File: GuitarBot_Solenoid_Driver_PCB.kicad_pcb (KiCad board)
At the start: 2 copper layers, 123.2 x 109.2 mm, 89 parts, among them J3V3 Screw_Terminal_01x02, Q1 NMOS, Q10 NMOS, Q11 NMOS, Q12 NMOS, Q13 NMOS, Q14 NMOS, Q15 NMOS, Q16 NMOS, Q2 NMOS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

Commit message: fixed labels:
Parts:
- moved D8 3.03 mm to (153.7, 99.1)
- moved D7 2.60 mm to (153.7, 105.5)
- moved D9 2.22 mm to (153.7, 92.7)
- moved D6 2.17 mm to (153.7, 112.0)
- moved D10 1.90 mm to (153.7, 86.2)
- moved D5 1.73 mm to (153.7, 118.4)
- moved D11 1.58 mm to (153.7, 79.8)
- moved D4 1.30 mm to (153.7, 124.8)
- moved D12 1.27 mm to (153.7, 73.4)
- moved D13 0.95 mm to (153.7, 66.9)
- moved D3 0.87 mm to (153.7, 131.3)
- moved D14 0.63 mm to (153.7, 60.5)
- moved D2 0.43 mm to (153.7, 137.7)
- moved D15 0.32 mm to (153.7, 54.1)
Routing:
- net Net-(D1-A): track 31.0 -> 32.0 mm
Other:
- board text added: "3V3"
- board text added: "GuitarBot Solenoid Actuation Module v 2 . 0 . 0 Northwestern University"
- board text added: "K"
- board text added: "SOL GND"
- board text removed: "GuitarBot Solenoid Actuation Module v 1 . 0 . 0 Northwestern University"
- board text removed: "VCC"
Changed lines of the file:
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@@
 	(footprint "Diode_THT:D_DO-201AD_P12.70mm_Horizontal"
 		(layer "F.Cu")
-		(at 153.67 54.395 180)
+		(at 153.67 54.078333 180)
 		(descr "Diode, DO-201AD series, Axial, Horizontal, pin pitch=12.7mm, length*diameter=9.5*5.2mm^2, http://www.diodes.com/_files/packages/DO-201AD.pdf")
 		(tags "Diode DO-201AD series Axial Horizontal pin pitch 12.7mm  length 9.5mm diameter 5.2mm")
@@
 		)
 		(fp_text user "K"
-			(at 0 -2.6 0)
+			(at -2.54 -1.886334 0)
 			(layer "F.SilkS")
 			(effects
@@
 		(tags "C Disc series Radial pin pitch 5.00mm diameter 11mm width 5.0mm Capacitor")
 		(property "Reference" "F1"
-			(at 2.5 -3.75 180)
+			(at -4.445 1.905 180)
 			(layer "F.SilkS")
 			(effects
@@
 		(tags "THT Terminal Block CUI TB007-508-16 pitch 5.08mm size 81.9x10.2mm drill 1.6mm pad 2.4mm")
 		(property "Reference" "JSOL2"
-			(at 38.4 -6.02 90)
+			(at 38.4 3.175 90)
 			(layer "F.SilkS")
 			(effects
@@
 	(footprint "Diode_THT:D_DO-201AD_P12.70mm_Horizontal"
 		(layer "F.Cu")
-		(at 153.67 108.145 180)
+		(at 153.67 105.545 180)
 		(descr "Diode, DO-201AD series, Axial, Horizontal, pin pitch=12.7mm, length*diameter=9.5*5.2mm^2, http://www.diodes.com/_files/packages/DO-201AD.pdf")
 		(tags "Diode DO-201AD series Axial Horizontal pin pitch 12.7mm  length 9.5mm diameter 5.2mm")
@@
 	(footprint "Diode_THT:D_DO-201AD_P12.70mm_Horizontal"
 		(layer "F.Cu")
-		(at 153.67 138.145 180)
+		(at 153.67 137.711667 180)
 		(descr "Diode, DO-201AD series, Axial, Horizontal, pin pitch=12.7mm, length*diameter=9.5*5.2mm^2, http://www.diodes.com/_files/packages/DO-201AD.pdf")
 		(tags "Diode DO-201AD series Axial Horizontal pin pitch 12.7mm  length 9.5mm diameter 5.2mm")
@@
 	(footprint "Diode_THT:D_DO-201AD_P12.70mm_Horizontal"
 		(layer "F.Cu")
-		(at 153.67 74.645 180)
+		(at 153.67 73.378333 180)
 		(descr "Diode, DO-201AD series, Axial, Horizontal, pin pitch=12.7mm, length*diameter=9.5*5.2mm^2, http://www.diodes.com/_files/packages/DO-201AD.pdf")
 		(tags "Diode DO-201AD series Axial Horizontal pin pitch 12.7mm  length 9.5mm diameter 5.2mm")
@@
 		)
 		(fp_text user "K"
-			(at 0 -2.6 0)
+			(at -2.54 -1.890334 0)
 			(layer "F.SilkS")
 			(effects
@@
 	(footprint "Diode_THT:D_DO-201AD_P12.70mm_Horizontal"
 		(layer "F.Cu")
-		(at 153.67 132.145 180)
+		(at 153.67 131.278333 180)
 		(descr "Diode, DO-201AD series, Axial, Horizontal, pin pitch=12.7mm, length*diameter=9.5*5.2mm^2, http://www.diodes.com/_files/packages/DO-201AD.pdf")
 		(tags "Diode DO-201AD series Axial Horizontal pin pitch 12.7mm  length 9.5mm diameter 5.2mm")
@@
 	(footprint "Diode_THT:D_DO-201AD_P12.70mm_Horizontal"
 		(layer "F.Cu")
-		(at 153.67 88.145 180)
+		(at 153.67 86.245 180)
 		(descr "Diode, DO-201AD series, Axial, Horizontal, pin pitch=12.7mm, length*diameter=9.5*5.2mm^2, http://www.diodes.com/_files/packages/DO-201AD.pdf")
 		(tags "Diode DO-201AD series Axial Horizontal pin pitch 12.7mm  length 9.5mm diameter 5.2mm")
@@
 		)
 		(fp_text user "K"
-			(at 0 -2.6 0)
+			(at -2.54 -1.893 0)
 			(layer "F.SilkS")
 			(effects
@@
 	(footprint "Diode_THT:D_DO-201AD_P12.70mm_Horizontal"
 		(layer "F.Cu")
-		(at 153.67 81.395 180)
+		(at 153.67 79.811667 180)
 		(descr "Diode, DO-201AD series, Axial, Horizontal, pin pitch=12.7mm, length*diameter=9.5*5.2mm^2, http://www.diodes.com/_files/packages/DO-201AD.pdf")
 		(tags "Diode DO-201AD series Axial Horizontal pin pitch 12.7mm  length 9.5mm diameter 5.2mm")
@@
 		)
 		(fp_text user "K"
-			(at 0 -2.6 0)
+			(at -2.54 -1.891666 0)
 			(layer "F.SilkS")
 			(effects
@@
 	(footprint "Diode_THT:D_DO-201AD_P12.70mm_Horizontal"
 		(layer "F.Cu")
-		(at 153.67 102.145 180)
+		(at 153.67 99.111667 180)
 		(descr "Diode, DO-201AD series, Axial, Horizontal, pin pitch=12.7mm, length*diameter=9.5*5.2mm^2, http://www.diodes.com/_files/packages/DO-201AD.pdf")
 		(tags "Diode DO-201AD series Axial Horizontal pin pitch 12.7mm  length 9.5mm diameter 5.2mm")
@@
 			(at -162.26 44.47 0)
 			(layer "F.Fab")
+			(hide yes)
 			(effects
 				(font
@@
 	(footprint "Diode_THT:D_DO-201AD_P12.70mm_Horizontal"
 		(layer "F.Cu")
-		(at 153.67 61.145 180)
+		(at 153.67 60.511667 180)
 		(descr "Diode, DO-201AD series, Axial, Horizontal, pin pitch=12.7mm, length*diameter=9.5*5.2mm^2, http://www.diodes.com/_files/packages/DO-201AD.pdf")
 		(tags "Diode DO-201AD series Axial Horizontal pin pitch 12.7mm  length 9.5mm diameter 5.2mm")
@@
 		)
 		(fp_text user "K"
-			(at 0 -2.6 0)
+			(at -2.54 -1.887666 0)
 			(layer "F.SilkS")
 			(effects
@@
 	(footprint "Diode_THT:D_DO-201AD_P12.70mm_Horizontal"
 		(layer "F.Cu")
-		(at 153.67 120.145 180)
+		(at 153.67 118.411667 180)
 		(descr "Diode, DO-201AD series, Axial, Horizontal, pin pitch=12.7mm, length*diameter=9.5*5.2mm^2, http://www.diodes.com/_files/packages/DO-201AD.pdf")
 		(tags "Diode DO-201AD series Axial Horizontal pin pitch 12.7mm  length 9.5mm diameter 5.2mm")
@@
 	(footprint "Diode_THT:D_DO-201AD_P12.70mm_Horizontal"
 		(layer "F.Cu")
-		(at 153.67 94.895 180)
+		(at 153.67 92.678333 180)
 		(descr "Diode, DO-201AD series, Axial, Horizontal, pin pitch=12.7mm, length*diameter=9.5*5.2mm^2, http://www.diodes.com/_files/packages/DO-201AD.pdf")
 		(tags "Diode DO-201AD series Axial Horizontal pin pitch 12.7mm  length 9.5mm diameter 5.2mm")
@@
 	(footprint "Diode_THT:D_DO-201AD_P12.70mm_Horizontal"
 		(layer "F.Cu")
-		(at 153.67 67.895 180)
+		(at 153.67 66.945 180)
 		(descr "Diode, DO-201AD series, Axial, Horizontal, pin pitch=12.7mm, length*diameter=9.5*5.2mm^2, http://www.diodes.com/_files/packages/DO-201AD.pdf")
 		(tags "Diode DO-201AD series Axial Horizontal pin pitch 12.7mm  length 9.5mm diameter 5.2mm")
@@
 		)
 		(fp_text user "K"
-			(at 0 -2.6 0)
+			(at -2.54 -1.889 0)
 			(layer "F.SilkS")
 			(effects
@@
 	(footprint "Diode_THT:D_DO-201AD_P12.70mm_Horizontal"
 		(layer "F.Cu")
-		(at 153.67 114.145 180)
+		(at 153.67 111.978333 180)
 		(descr "Diode, DO-201AD series, Axial, Horizontal, pin pitch=12.7mm, length*diameter=9.5*5.2mm^2, http://www.diodes.com/_files/packages/DO-201AD.pdf")
 		(tags "Diode DO-201AD series Axial Horizontal pin pitch 12.7mm  length 9.5mm diameter 5.2mm")
@@
 		)
 		(fp_text user "K"
-			(at 0 -2.6 0)
+			(at -2.54 -1.885 0)
 			(layer "F.SilkS")
 			(effects
@@
 	(footprint "Diode_THT:D_DO-201AD_P12.70mm_Horizontal"
 		(layer "F.Cu")
-		(at 153.67 126.145 180)
+		(at 153.67 124.845 180)
 		(descr "Diode, DO-201AD series, Axial, Horizontal, pin pitch=12.7mm, length*diameter=9.5*5.2mm^2, http://www.diodes.com/_files/packages/DO-201AD.pdf")
 		(tags "Diode DO-201AD series Axial Horizontal pin pitch 12.7mm  length 9.5mm diameter 5.2mm")
@@
 		)
 	)
-	(gr_text "VCC"
+	(gr_text "3V3"
 		(at 79.2 49.975 90)
 		(layer "F.SilkS")
@@
 		)
 	)
+	(gr_text "K"
+		(at 156.21 113.876667 0)
+		(layer "F.SilkS")
+		(effects
+			(font
+				(size 1 1)
+				(thickness 0.15)
+			)
+		)
+	)
 	(gr_text "INTA"
 		(at 81.95 138.25 90)
@@
 		)
 	)
+	(gr_text "K"
+		(at 156.21 126.746 0)
+		(layer "F.SilkS")
+		(effects
+			(font
+				(size 1 1)
+				(thickness 0.15)
+			)
+		)
+	)
+	(gr_text "K"
+		(at 156.21 94.572667 0)
+		(layer "F.SilkS")
+		(effects
+			(font
+				(size 1 1)
+				(thickness 0.15)
+			)
+		)
+	)
+	(gr_text "K"
+		(at 156.21 120.311333 0)
+		(layer "F.SilkS")
+		(effects
+			(font
+				(size 1 1)
+				(thickness 0.15)
+			)
+		)
+	)
 	(gr_text "Solenoid Power\n"
 		(at 169.808 77.335901 270)
@@
 		)
 	)
+	(gr_text "K"
+		(at 156.21 133.180667 0)
+		(layer "F.SilkS")
+		(effects
+			(font
+				(size 1 1)
+				(thickness 0.15)
+			)
+		)
+	)
 	(gr_text "12V+\n"
 		(at 134.62 51.435 90)
@@
 		)
 	)
-	(gr_text "GuitarBot Solenoid Actuation Module\nv 1 . 0 . 0\nNorthwestern\nUniversity"
+	(gr_text "GuitarBot Solenoid Actuation Module\nv 2 . 0 . 0\nNorthwestern\nUniversity"
 		(at 63.754 73.914 90)
 		(layer "F.SilkS")
@@
 		)
 	)
+	(gr_text "K"
+		(at 156.21 139.615333 0)
+		(layer "F.SilkS")
+		(effects
+			(font
+				(size 1 1)
+				(thickness 0.15)
+			)
+		)
+	)
+	(gr_text "SOL GND"
+		(at 128.905 137.16 0)
+		(layer "F.SilkS")
+		(effects
+			(font
+				(size 1 1)
+				(thickness 0.15)
+			)
+			(justify left bottom)
+		)
+	)
 	(gr_text "CERAS"
 		(at 57.15 69.85 90)
@@
 		)
 	)
+	(gr_text "K"
+		(at 156.21 101.007333 0)
+		(layer "F.SilkS")
+		(effects
+			(font
+				(size 1 1)
+				(thickness 0.15)
+			)
+		)
+	)
+	(gr_text "K"
+		(at 156.21 107.442 0)
+		(layer "F.SilkS")
+		(effects
+			(font
+				(size 1 1)
+				(thickness 0.15)
+			)
+		)
+	)
 	(gr_text "INTB"
 		(at 79.375 138.225 90)
@@
 		)
 	)
+	(gr_text "K"
+		(at 156.21 146.05 0)
+		(layer "F.SilkS")
+		(effects
+			(font
+				(size 1 1)
+				(thickness 0.15)
+			)
+		)
+	)
 	(gr_text "GND\n\n"
 		(at 83.725 50.075 90)
@@
 	)
 	(segment
-		(start 132.08 134.27)
+		(start 132.08 135.255)
 		(end 132.08 131.28)
 		(width 1.016)
@@
 	)
 	(segment
-		(start 120.65 141.062667)
-		(end 130.432667 131.28)
+		(start 140.97 144.145)
+		(end 132.08 135.255)
 		(width 1.016)
 		(layer "F.Cu")
@@
 	)
 	(segment
-		(start 130.432667 131.28)
-		(end 132.08 131.28)
+		(start 120.65 141.062667)
+		(end 130.432667 131.28)
 		(width 1.016)
 		(layer "F.Cu")
@@
 	)
 	(segment
-		(start 140.97 143.16)
-		(end 132.08 134.27)
+		(start 130.432667 131.28)
+		(end 132.08 131.28)
 		(width 1.016)
 		(layer "F.Cu")

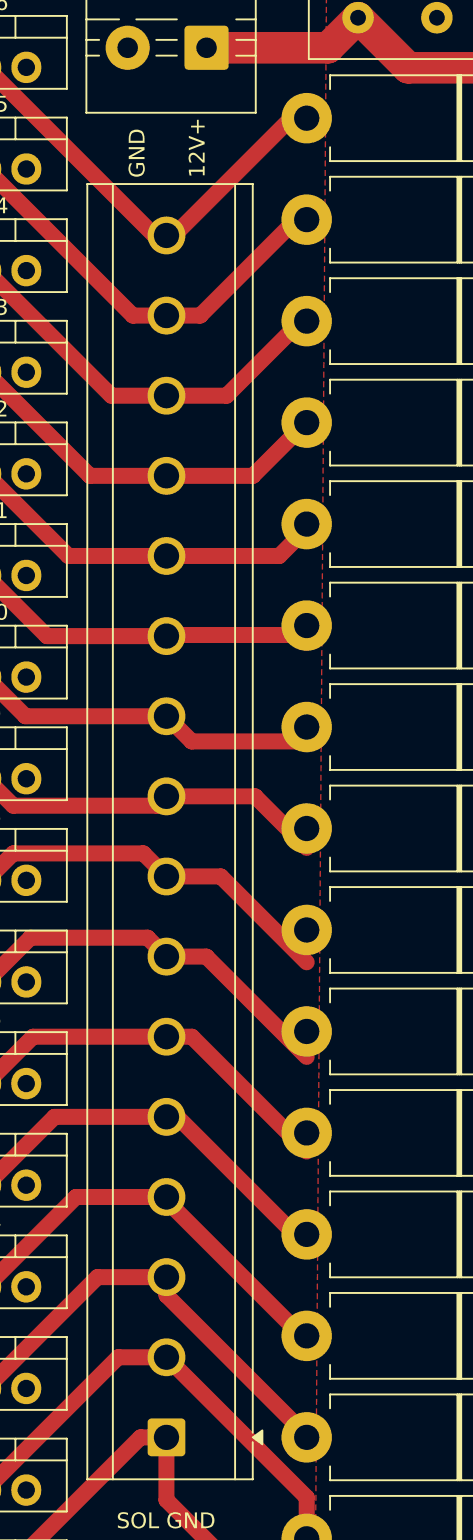
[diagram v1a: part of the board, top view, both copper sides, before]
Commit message: fixed traces
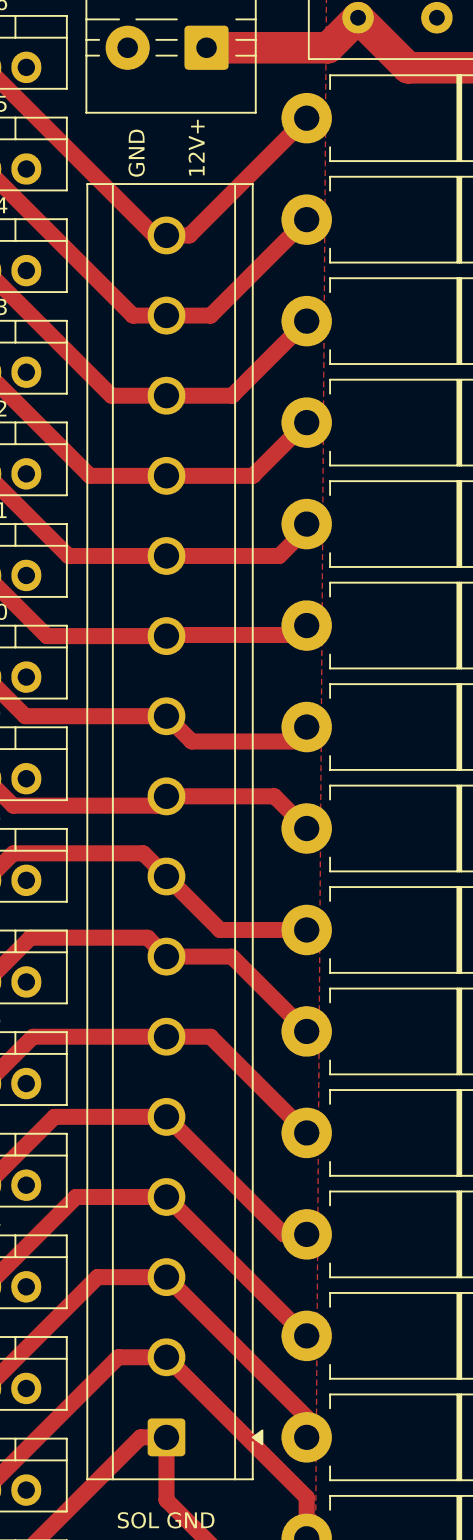
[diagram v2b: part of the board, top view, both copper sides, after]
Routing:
- net Net-(D8-A): track 23.9 -> 23.0 mm
- net Net-(D7-A): track 24.6 -> 23.9 mm
- net Net-(D9-A): track 22.6 -> 22.1 mm
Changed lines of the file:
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@@
+	)
+	(segment
+		(start 132.08 121.12)
+		(end 140.97 130.01)
+		(width 1.016)
+		(layer "F.Cu")
+		(net 5)
 	)
 	(segment
@@
 	)
 	(segment
-		(start 140.97 131.16)
-		(end 132.08 122.27)
-		(width 1.016)
-		(layer "F.Cu")
-		(net 5)
-	)
-	(segment
 		(start 127.707334 121.12)
 		(end 132.08 121.12)
@@
 	)
 	(segment
-		(start 132.08 122.27)
-		(end 132.08 121.12)
+		(start 140.97 130.01)
+		(end 140.97 131.278333)
 		(width 1.016)
 		(layer "F.Cu")
@@
 	)
 	(segment
-		(start 140.97 125.16)
-		(end 132.08 116.27)
-		(width 1.016)
-		(layer "F.Cu")
-		(net 6)
-	)
-	(segment
 		(start 120.65 121.734667)
 		(end 126.344667 116.04)
@@
 	)
 	(segment
-		(start 132.08 116.27)
-		(end 132.08 116.04)
+		(start 132.08 116.04)
+		(end 140.885 124.845)
 		(width 1.016)
 		(layer "F.Cu")
 		(net 6)
+	)
+	(segment
+		(start 140.885 124.845)
+		(end 140.97 124.845)
+		(width 1.016)
+		(layer "F.Cu")
+		(net 6)
+	)
+	(segment
+		(start 132.08 110.96)
+		(end 139.531667 118.411667)
+		(width 1.016)
+		(layer "F.Cu")
+		(net 7)
 	)
 	(segment
@@
 	)
 	(segment
-		(start 140.97 119.16)
-		(end 132.77 110.96)
-		(width 1.016)
-		(layer "F.Cu")
-		(net 7)
-	)
-	(segment
-		(start 132.77 110.96)
-		(end 132.08 110.96)
+		(start 139.531667 118.411667)
+		(end 140.97 118.411667)
 		(width 1.016)
 		(layer "F.Cu")
@@
 	)
 	(segment
-		(start 133.69 105.88)
-		(end 132.08 105.88)
+		(start 132.08 105.88)
+		(end 134.871667 105.88)
 		(width 1.016)
 		(layer "F.Cu")
@@
 	)
 	(segment
-		(start 140.97 113.16)
-		(end 133.69 105.88)
+		(start 134.871667 105.88)
+		(end 140.97 111.978333)
 		(width 1.016)
 		(layer "F.Cu")
 		(net 8)
+	)
+	(segment
+		(start 136.225 100.8)
+		(end 140.97 105.545)
+		(width 1.016)
+		(layer "F.Cu")
+		(net 9)
 	)
 	(segment
@@
 	)
 	(segment
-		(start 134.61 100.8)
-		(end 132.08 100.8)
-		(width 1.016)
-		(layer "F.Cu")
-		(net 9)
-	)
-	(segment
 		(start 123.461667 99.6)
 		(end 130.88 99.6)
@@
 	)
 	(segment
-		(start 140.97 107.16)
-		(end 134.61 100.8)
+		(start 132.08 100.8)
+		(end 136.225 100.8)
 		(width 1.016)
 		(layer "F.Cu")
@@
 	)
 	(segment
+		(start 135.471667 99.111667)
+		(end 140.97 99.111667)
+		(width 1.016)
+		(layer "F.Cu")
+		(net 10)
+	)
+	(segment
+		(start 132.08 95.72)
+		(end 135.471667 99.111667)
+		(width 1.016)
+		(layer "F.Cu")
+		(net 10)
+	)
+	(segment
 		(start 120.655 95.964)
 		(end 122.364 94.255)
@@
 	)
 	(segment
-		(start 135.53 95.72)
-		(end 132.08 95.72)
-		(width 1.016)
-		(layer "F.Cu")
-		(net 10)
-	)
-	(segment
-		(start 140.97 101.16)
-		(end 135.53 95.72)
-		(width 1.016)
-		(layer "F.Cu")
-		(net 10)
+		(start 138.931667 90.64)
+		(end 140.97 92.678333)
+		(width 1.016)
+		(layer "F.Cu")
+		(net 11)
 	)
 	(segment
@@
 	)
 	(segment
-		(start 137.7 90.64)
-		(end 132.08 90.64)
+		(start 132.08 90.64)
+		(end 138.931667 90.64)
 		(width 1.016)
 		(layer "F.Cu")
@@
 	)
 	(segment
-		(start 140.97 93.91)
-		(end 137.7 90.64)
-		(width 1.016)
-		(layer "F.Cu")
-		(net 11)
-	)
-	(segment
 		(start 133.68 87.16)
 		(end 132.08 85.56)
@@
 	)
 	(segment
-		(start 135.89 65.24)
-		(end 132.08 65.24)
-		(width 1.016)
-		(layer "F.Cu")
-		(net 16)
-	)
-	(segment
 		(start 128.587 65.24)
 		(end 132.08 65.24)
@@
 	)
 	(segment
-		(start 140.97 60.16)
-		(end 135.89 65.24)
+		(start 136.241667 65.24)
+		(end 140.97 60.511667)
 		(width 1.016)
 		(layer "F.Cu")
@@
 	)
 	(segment
-		(start 134.22 60.16)
-		(end 132.08 60.16)
+		(start 132.08 65.24)
+		(end 136.241667 65.24)
+		(width 1.016)
+		(layer "F.Cu")
+		(net 16)
+	)
+	(segment
+		(start 134.888333 60.16)
+		(end 140.97 54.078333)
 		(width 1.016)
 		(layer "F.Cu")
@@
 	)
 	(segment
-		(start 140.97 53.41)
-		(end 134.22 60.16)
-		(width 1.016)
-		(layer "F.Cu")
-		(net 17)
-	)
-	(segment
 		(start 120.655 50.865334)
 		(end 129.949666 60.16)
@@
 	)
 	(segment
+		(start 132.08 60.16)
+		(end 134.888333 60.16)
+		(width 1.016)
+		(layer "F.Cu")
+		(net 17)
+	)
+	(segment
+		(start 133.535 55.08)
+		(end 140.97 47.645)
+		(width 1.016)
+		(layer "F.Cu")
+		(net 18)
+	)
+	(segment
+		(start 132.08 55.08)
+		(end 133.535 55.08)
+		(width 1.016)
+		(layer "F.Cu")
+		(net 18)
+	)
+	(segment
 		(start 120.655 44.422667)
 		(end 131.312333 55.08)
 		(width 1.016)
 		(layer "F.Cu")
-		(net 18)
-	)
-	(segment
-		(start 132.55 55.08)
-		(end 132.08 55.08)
-		(width 1.016)
-		(layer "F.Cu")
-		(net 18)
-	)
-	(segment
-		(start 140.97 46.66)
-		(end 132.55 55.08)
-		(width 1.016)
-		(layer "F.Cu")
